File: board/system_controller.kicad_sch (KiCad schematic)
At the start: 7 parts, among them U301 ATmega808-M, Y301 32K768

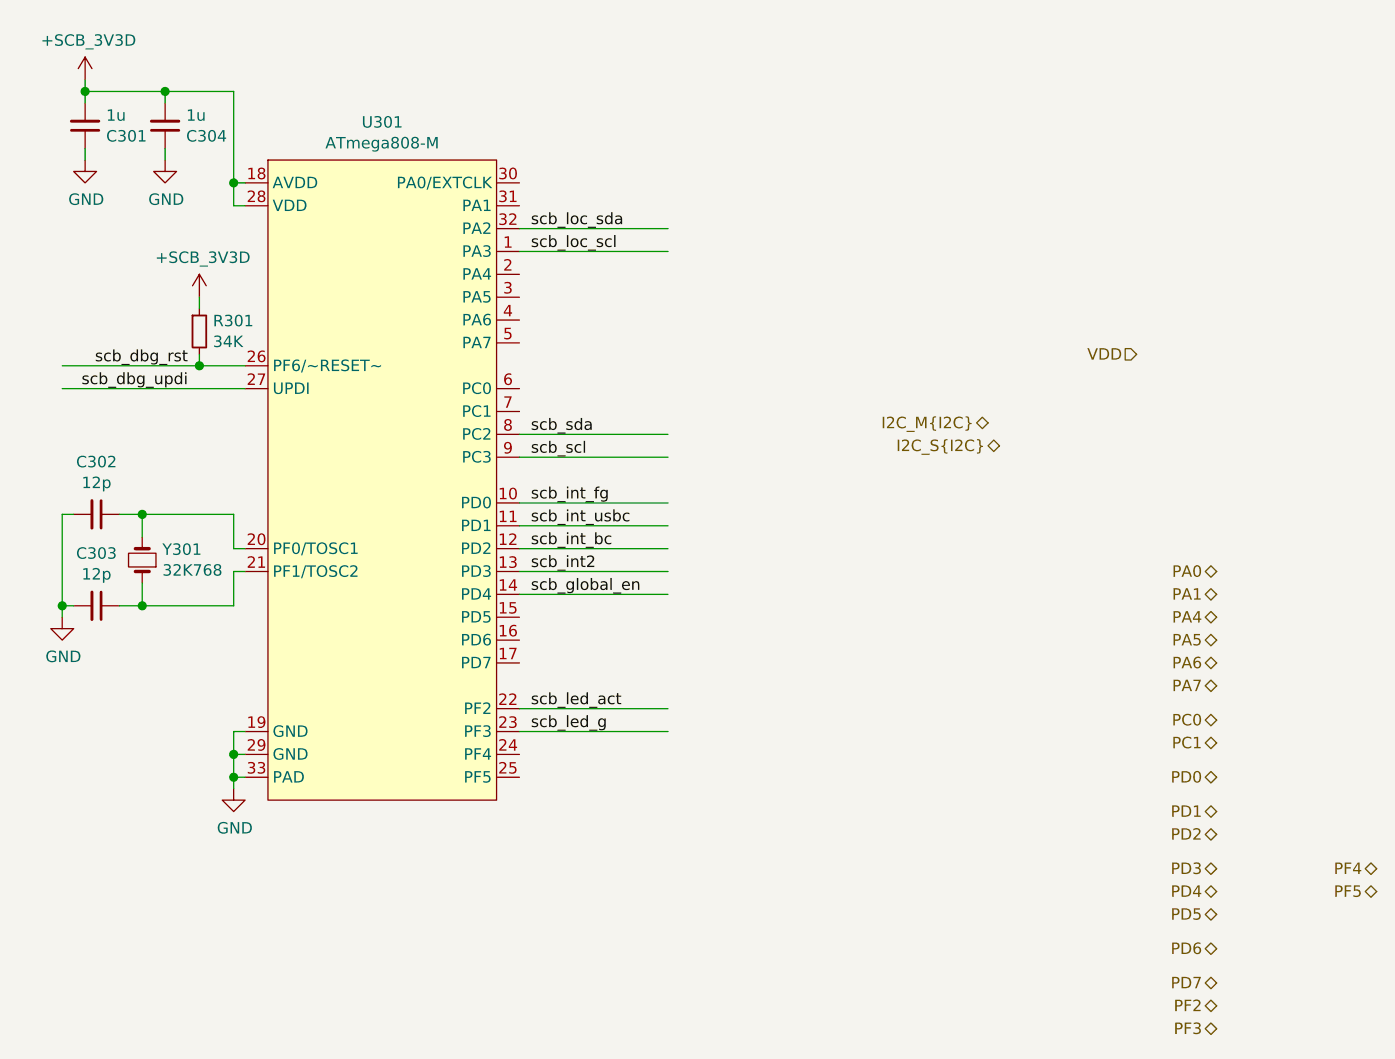
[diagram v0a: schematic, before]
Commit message: Added testpoints and other fixes
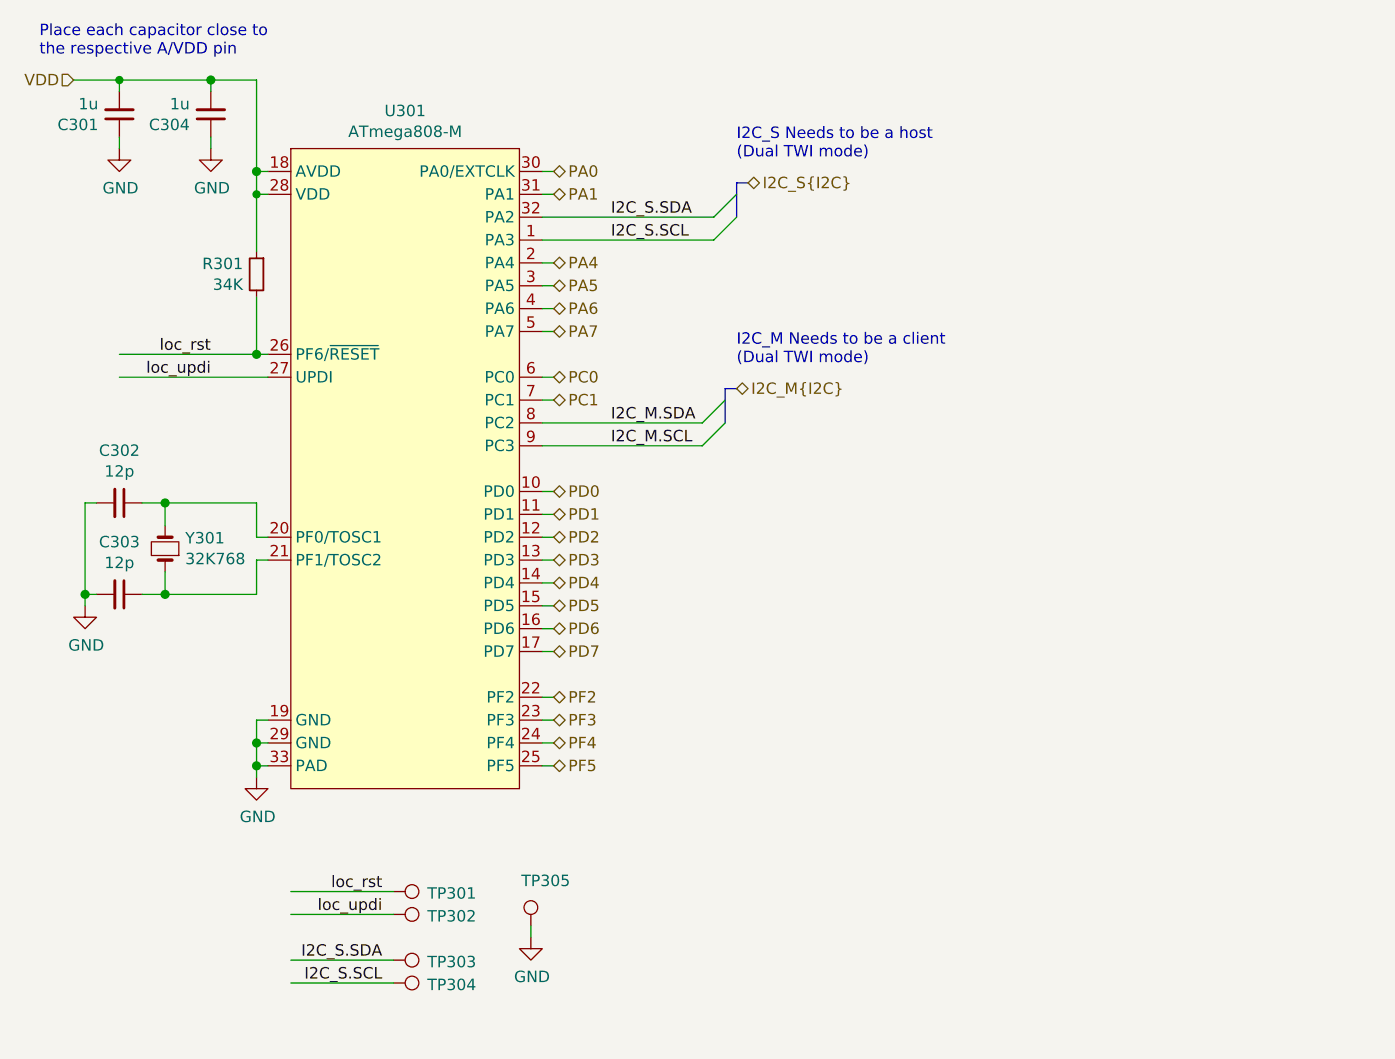
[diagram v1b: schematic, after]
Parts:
- added TP301, TP302, TP303, TP304, TP305: TestPoint, DIYPie:TestPoint_Pad_D1.5mm, symbol DIYPie:TestPoint
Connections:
- net +3V3 is gone; now on net VDD: C301.2, C304.2, R301.1, U301.18 (AVDD), U301.28 (VDD)
- net scb_global_en is gone; now on net PD4: U301.14 (PD4)
- net scb_int2 is gone; now on net PD3: U301.13 (PD3)
- net scb_int_bc is gone; now on net PD2: U301.12 (PD2)
- net scb_int_fg is gone; now on net PD0: U301.10 (PD0)
- net scb_int_usbc is gone; now on net PD1: U301.11 (PD1)
- net scb_led_act is gone; now on net PF2: U301.22 (PF2)
- net scb_led_g is gone; now on net PF3: U301.23 (PF3)
- net GND: now also TP305.1
- net PA0: now also U301.30 (PA0/EXTCLK)
- net PA1: now also U301.31 (PA1)
- net PA4: now also U301.2 (PA4)
- net PA5: now also U301.3 (PA5)
- net PA6: now also U301.4 (PA6)
- net PA7: now also U301.5 (PA7)
- net PC0: now also U301.6 (PC0)
- net PC1: now also U301.7 (PC1)
- net PD5: now also U301.15 (PD5)
- net PD6: now also U301.16 (PD6)
- net PD7: now also U301.17 (PD7)
- net PF4: now also U301.24 (PF4)
- net PF5: now also U301.25 (PF5)
- net scb_dbg_rst renamed loc_rst
- net loc_rst: now also TP301.1
- net scb_dbg_updi renamed loc_updi
- net loc_updi: now also TP302.1
- net scb_loc_scl renamed I2C_S.SCL
- net I2C_S.SCL: now also TP304.1
- net scb_loc_sda renamed I2C_S.SDA
- net I2C_S.SDA: now also TP303.1
- net scb_scl renamed I2C_M.SCL
- net scb_sda renamed I2C_M.SDA
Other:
- note added: "I2C_M Needs to be a client (Dual TWI mode)"
- note added: "I2C_S Needs to be a host (Dual TWI mode)"
- note added: "Place each capacitor close to the respective A/VDD pin"
- moved on the sheet: C301, C302, C303, C304, R301, U301, Y301
